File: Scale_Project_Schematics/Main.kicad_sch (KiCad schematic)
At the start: 13 parts, among them J10 LCD 2, J11 Keypad, J12 Power, J17 Lcd 3, J7 AVR-ISP-6, J8 Loadcell, J9 LCD 1, SW1 SW_MEC_5E, U2 ATmega328-P, Y2 Crystal

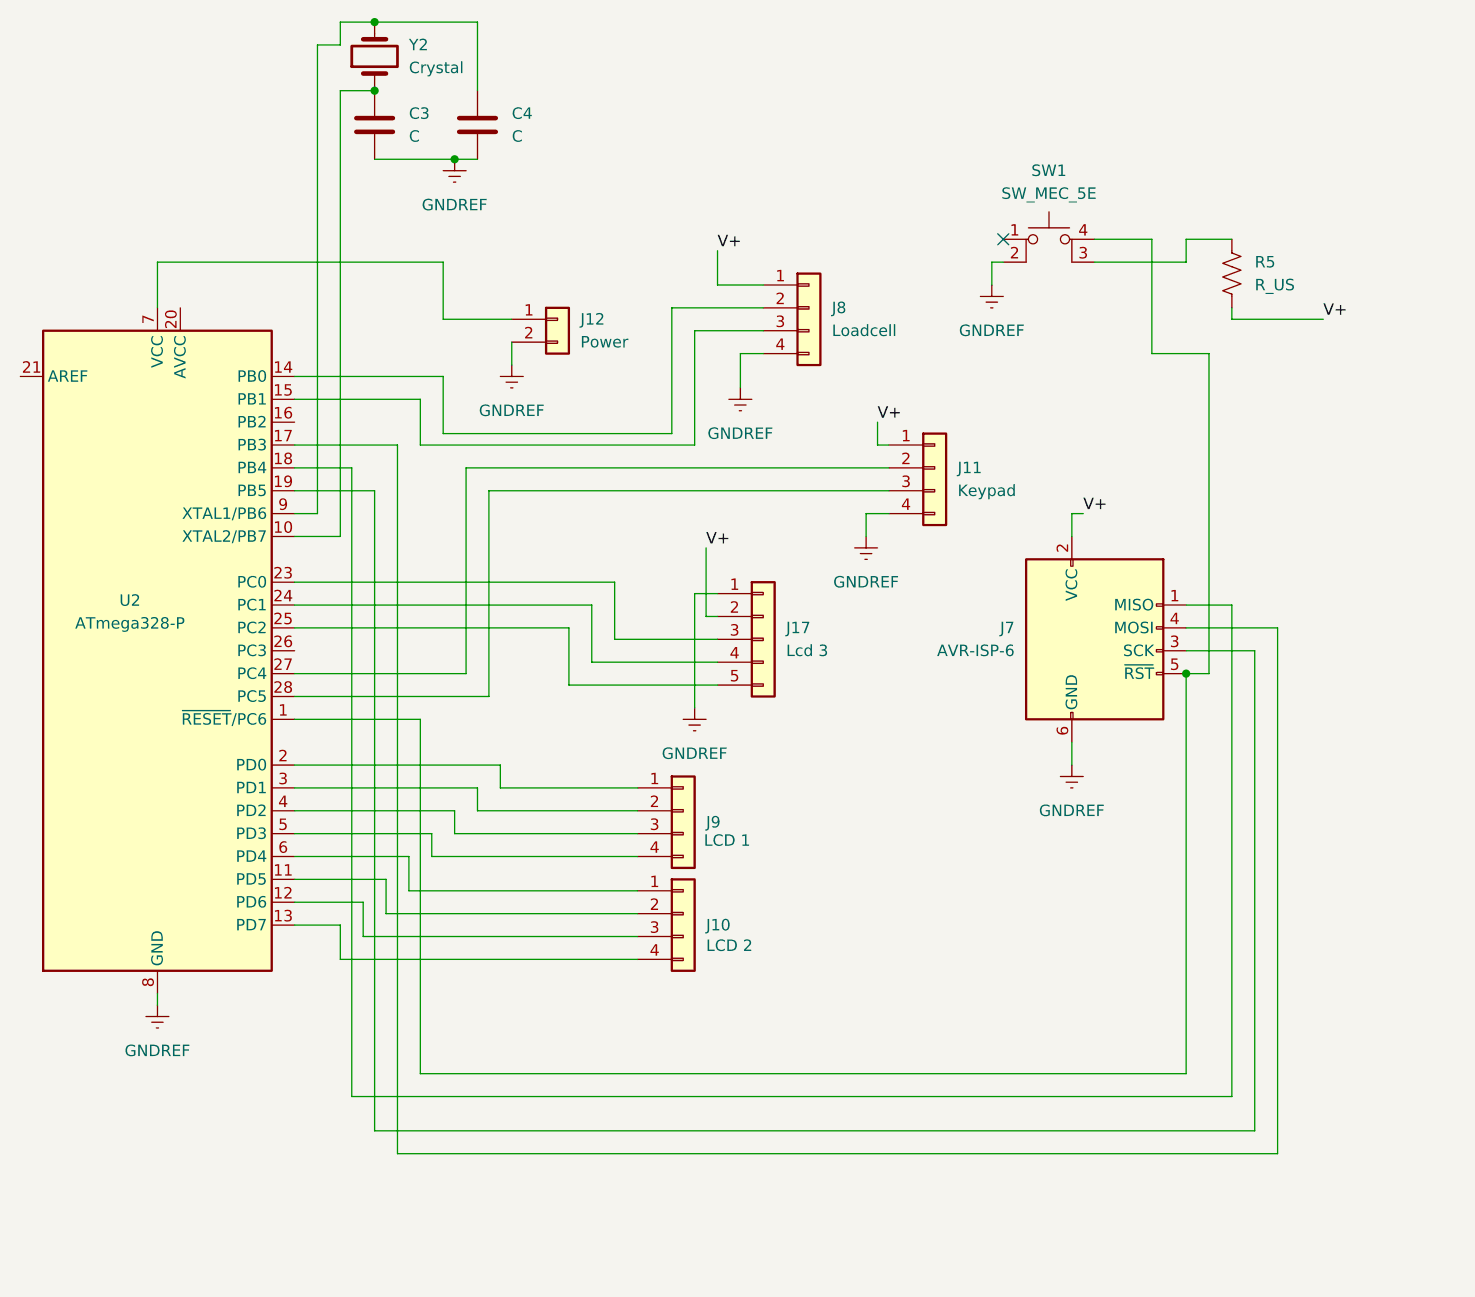
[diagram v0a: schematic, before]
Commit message: Adds Power sheet
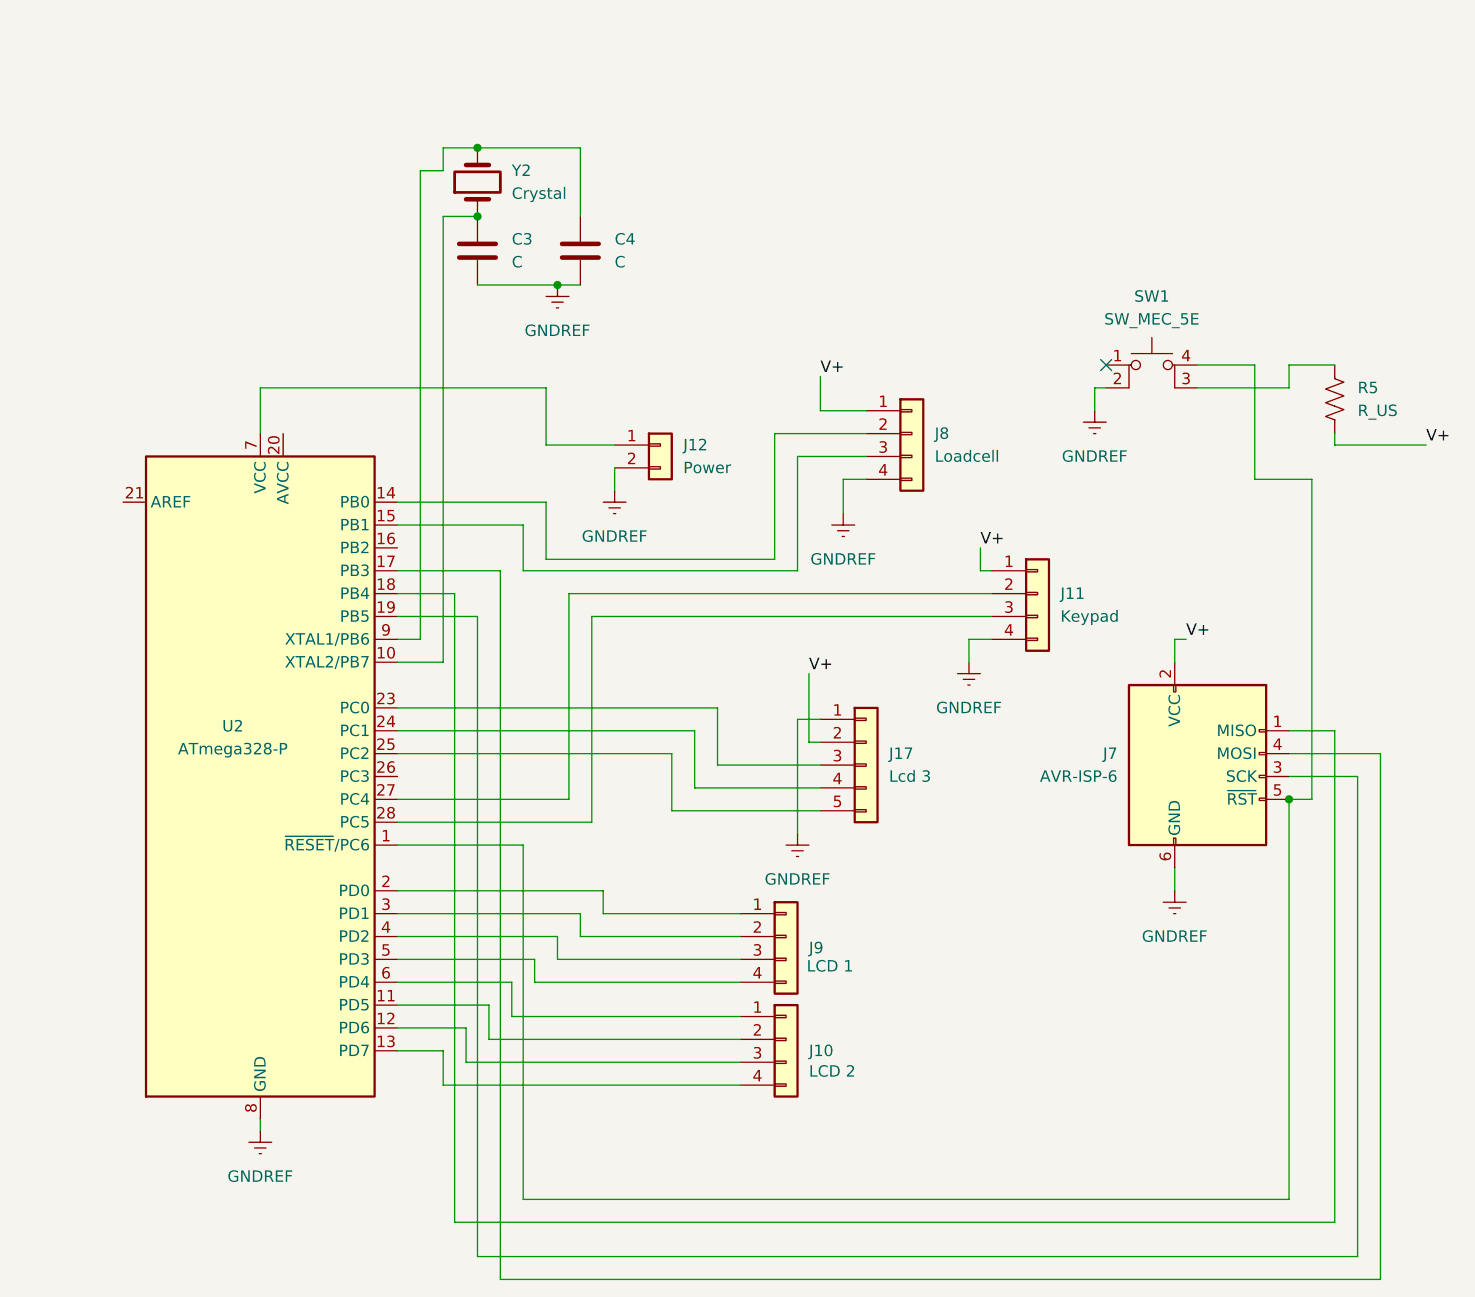
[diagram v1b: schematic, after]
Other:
- moved on the sheet: C3, C4, J10, J11, J12, J17, J7, J8, J9, R5, SW1, U2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
